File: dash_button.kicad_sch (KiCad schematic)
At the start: 55 parts, among them J1 1050570001, J2 MINI 5PTP, J3 Debug, J4 JST PH 1x2, J5 JST PH 1x5, P1 CONN_02X03, Q1 AO3401A, Q2 AO3401A, Q3 AO3401A, Q4 AO3401A, Q5 AO3401A, Q6 AO3401A, SW1 SW_Push, SW2 SW_Push, SW3 SW_Push, SW4 SW_Push, SW5 SW_Push, U1 ATtiny441-M, U2 HT7550-1

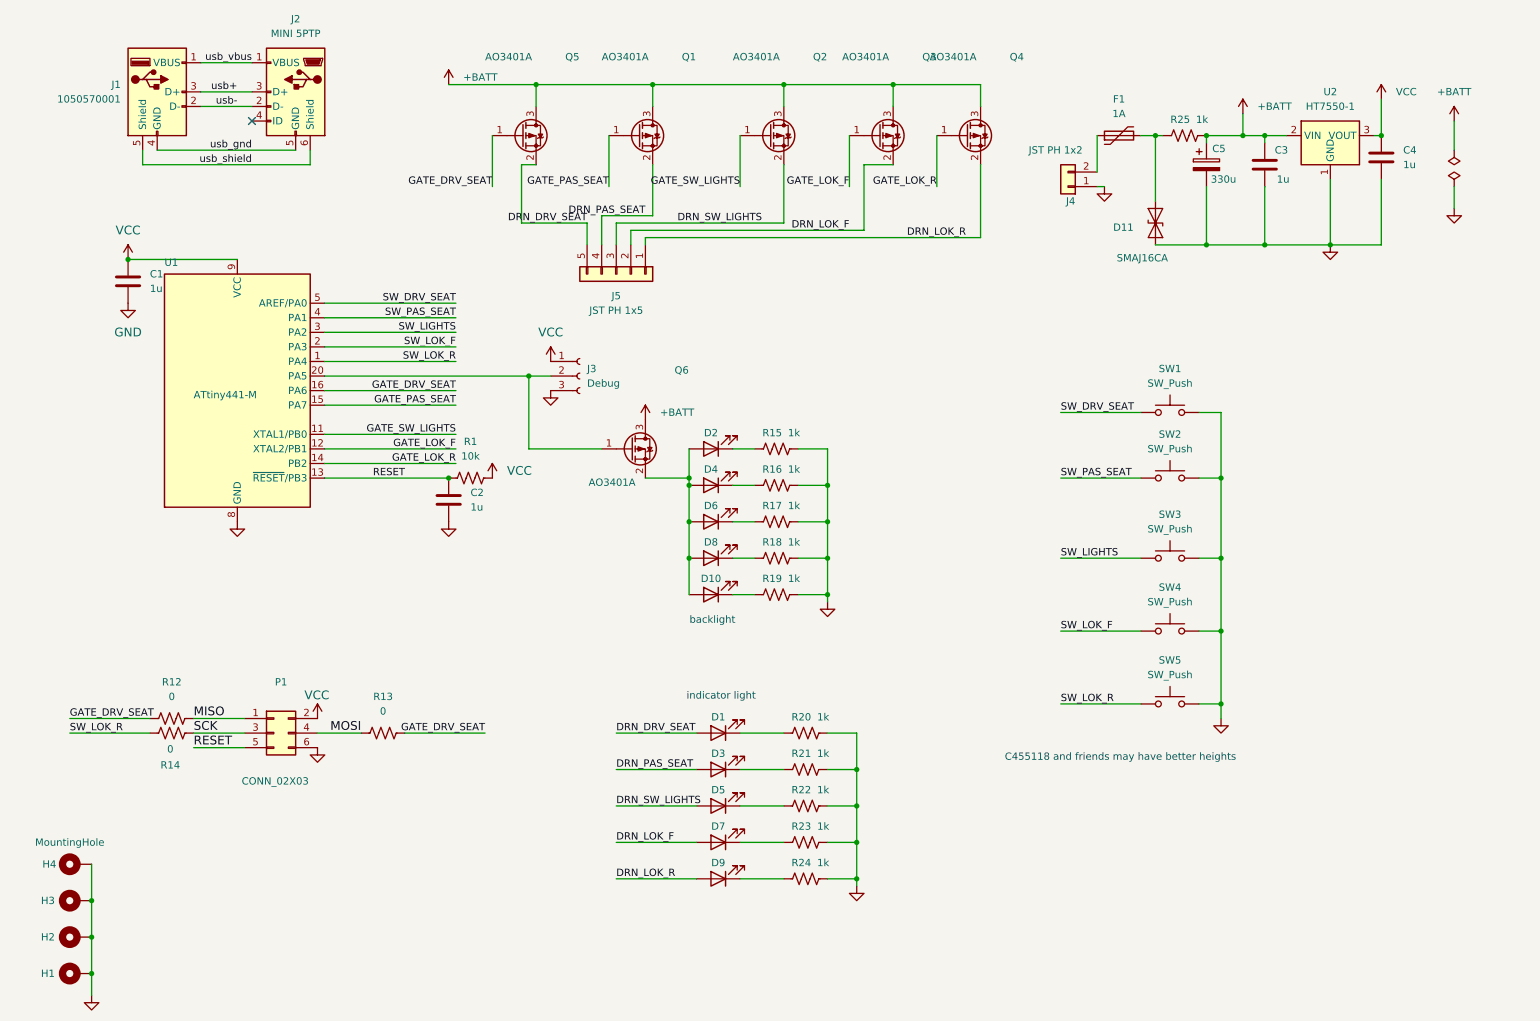
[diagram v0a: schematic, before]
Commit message: add automation for generating board_files
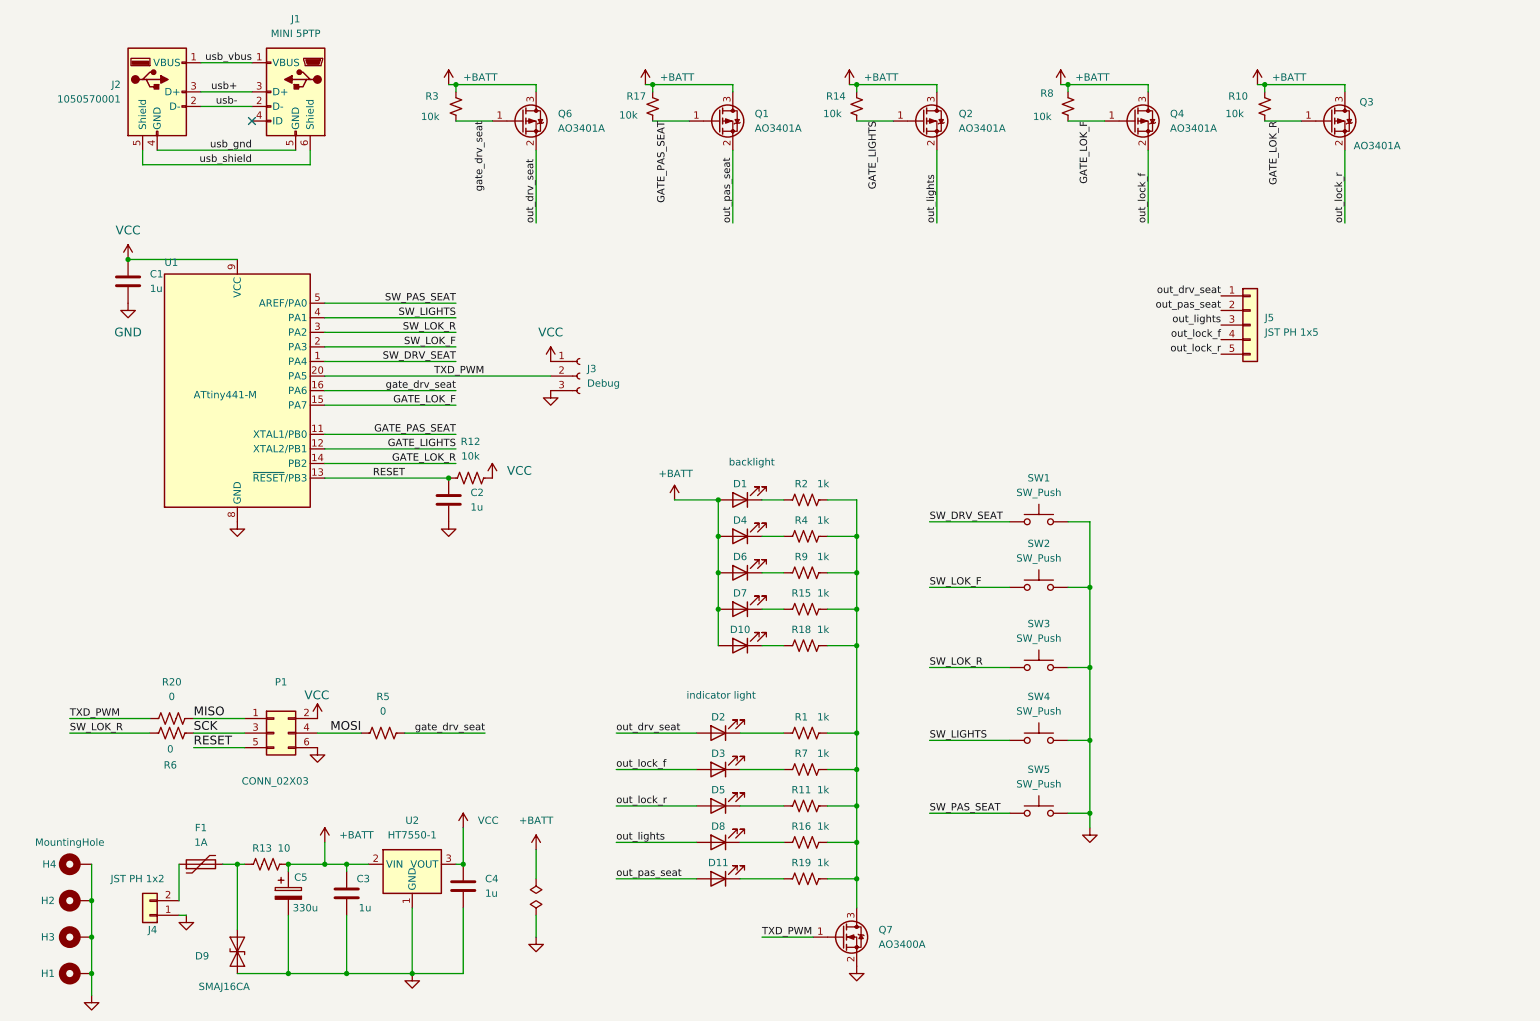
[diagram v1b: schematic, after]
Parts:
- removed Q1, Q2, Q4, Q5, Q6: AO3401A, Package_TO_SOT_SMD:SOT-23, symbol Device:Q_PMOS_GSD
- added Q1, Q2, Q4, Q6: AO3401A, Package_TO_SOT_SMD:SOT-23, symbol Transistor_FET:AO3401A
- added Q7: AO3400A, Package_TO_SOT_SMD:SOT-23, symbol Transistor_FET:AO3400A
- added R10, R14, R17, R3, R8: 10k, Resistor_SMD:R_0805_2012Metric_Pad1.20x1.40mm_HandSolder, symbol Device:R_Small_US
- Q3: Manufacturer Alpha & Omega Semicon -> Alpha & Omega Semicon
- R1: renamed from R20; footprint Resistor_SMD:R_0402_1005Metric -> Resistor_SMD:R_0805_2012Metric_Pad1.20x1.40mm_HandSolder; LCSC Part # C11702 -> C17513; MPN 0402WGF1001TCE -> 0805W8F1001T5E
- R11: renamed from R22; footprint Resistor_SMD:R_0402_1005Metric -> Resistor_SMD:R_0805_2012Metric_Pad1.20x1.40mm_HandSolder; LCSC Part # C11702 -> C17513; MPN 0402WGF1001TCE -> 0805W8F1001T5E
- R12: renamed from R1; footprint Resistor_SMD:R_0402_1005Metric -> Resistor_SMD:R_0805_2012Metric_Pad1.20x1.40mm_HandSolder; LCSC Part # C25744 -> C17414; MPN 0402WGF1002TCE -> 0805W8F1002T5E
- R13: renamed from R25; value 1k -> 10; footprint Resistor_SMD:R_0402_1005Metric -> Resistor_SMD:R_0805_2012Metric_Pad1.20x1.40mm_HandSolder; LCSC Part # C11702 -> C17415; MPN 0402WGF1001TCE -> 0805W8F100JT5E
- R15: renamed from R18; footprint Resistor_SMD:R_0402_1005Metric -> Resistor_SMD:R_0805_2012Metric_Pad1.20x1.40mm_HandSolder; LCSC Part # C11702 -> C17513; MPN 0402WGF1001TCE -> 0805W8F1001T5E
- R16: renamed from R23; footprint Resistor_SMD:R_0402_1005Metric -> Resistor_SMD:R_0805_2012Metric_Pad1.20x1.40mm_HandSolder; LCSC Part # C11702 -> C17513; MPN 0402WGF1001TCE -> 0805W8F1001T5E
- R18: renamed from R19; footprint Resistor_SMD:R_0402_1005Metric -> Resistor_SMD:R_0805_2012Metric_Pad1.20x1.40mm_HandSolder; LCSC Part # C11702 -> C17513; MPN 0402WGF1001TCE -> 0805W8F1001T5E
- R19: renamed from R24; footprint Resistor_SMD:R_0402_1005Metric -> Resistor_SMD:R_0805_2012Metric_Pad1.20x1.40mm_HandSolder; LCSC Part # C11702 -> C17513; MPN 0402WGF1001TCE -> 0805W8F1001T5E
- R2: renamed from R15; footprint Resistor_SMD:R_0402_1005Metric -> Resistor_SMD:R_0805_2012Metric_Pad1.20x1.40mm_HandSolder; LCSC Part # C11702 -> C17513; MPN 0402WGF1001TCE -> 0805W8F1001T5E
- R20: renamed from R12; footprint Resistor_SMD:R_0402_1005Metric -> Resistor_SMD:R_0805_2012Metric_Pad1.20x1.40mm_HandSolder; LCSC Part # C17168 -> C17477; MPN 0402WGF0000TCE -> 0805W8F0000T5E
- R4: renamed from R16; footprint Resistor_SMD:R_0402_1005Metric -> Resistor_SMD:R_0805_2012Metric_Pad1.20x1.40mm_HandSolder; LCSC Part # C11702 -> C17513; MPN 0402WGF1001TCE -> 0805W8F1001T5E
- R5: renamed from R13; footprint Resistor_SMD:R_0402_1005Metric -> Resistor_SMD:R_0805_2012Metric_Pad1.20x1.40mm_HandSolder; LCSC Part # C17168 -> C17477; MPN 0402WGF0000TCE -> 0805W8F0000T5E
- R6: renamed from R14; footprint Resistor_SMD:R_0402_1005Metric -> Resistor_SMD:R_0805_2012Metric_Pad1.20x1.40mm_HandSolder; LCSC Part # C17168 -> C17477; MPN 0402WGF0000TCE -> 0805W8F0000T5E
- R7: renamed from R21; footprint Resistor_SMD:R_0402_1005Metric -> Resistor_SMD:R_0805_2012Metric_Pad1.20x1.40mm_HandSolder; LCSC Part # C11702 -> C17513; MPN 0402WGF1001TCE -> 0805W8F1001T5E
- R9: renamed from R17; footprint Resistor_SMD:R_0402_1005Metric -> Resistor_SMD:R_0805_2012Metric_Pad1.20x1.40mm_HandSolder; LCSC Part # C11702 -> C17513; MPN 0402WGF1001TCE -> 0805W8F1001T5E
- U2: MPN (none) -> HT7550-1
- renumbered D2 to D1, D9 to D11, D1 to D2, D8 to D7, D7 to D8, D11 to D9, H3 to H2, H2 to H3, J2 to J1, J1 to J2
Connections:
- net GATE_SW_LIGHTS is gone; now on net GATE_PAS_SEAT: U1.11 (XTAL1/PB0)
- net +BATT: now also D1.2 (A), D10.2 (A), D4.2 (A), D6.2 (A), D7.2 (A), Q1.3 (D), Q2.3 (D), Q4.3 (D), Q6.3 (D), R10.1, R14.1, R17.1, R3.1, R8.1
- net GATE_LOK_F: now also U1.15 (PA7), Q4.1 (G), R8.2; no longer Q3.1 (G), U1.12 (XTAL2/PB1)
- net GATE_LOK_R: now also Q3.1 (G), R10.2
- net GATE_PAS_SEAT: now also Q1.1 (G), R17.2; no longer U1.15 (PA7)
- net GND: now also Q7.2 (S); no longer R1.2, R11.2, R15.2, R16.2, R18.2, R19.2, R2.2, R4.2, R7.2, R9.2
- net SW_DRV_SEAT: now also U1.1 (PA4); no longer U1.5 (AREF/PA0)
- net SW_LIGHTS: now also SW4.1, U1.4 (PA1); no longer SW3.1, U1.3 (PA2)
- net SW_LOK_F: now also SW2.1; no longer SW4.1
- net SW_LOK_R: now also SW3.1, U1.3 (PA2); no longer SW5.1, U1.1 (PA4)
- net SW_PAS_SEAT: now also SW5.1, U1.5 (AREF/PA0); no longer SW2.1, U1.4 (PA1)
- net TXD_PWM: now reaches J3.2 (Pin_2), U1.20 (PA5)
- net TXD_PWM: now also R20.2, Q7.1 (G)
- net DRN_DRV_SEAT renamed out_drv_seat
- net out_drv_seat: now also J5.1 (Pin_1), Q6.2 (S); no longer J5.5 (Pin_5)
- removed net DRN_LOK_F: D8.2 (A), J5.2 (Pin_2), Q3.2 (S)
- net DRN_LOK_R renamed out_pas_seat
- net out_pas_seat: now also J5.2 (Pin_2), Q1.2 (S); no longer J5.1 (Pin_1)
- net DRN_PAS_SEAT renamed out_lock_f
- net out_lock_f: now also Q4.2 (S)
- net DRN_SW_LIGHTS renamed out_lights
- net out_lights: now also D8.2 (A), Q2.2 (S); no longer D5.2 (A)
- net GATE_DRV_SEAT renamed gate_drv_seat
- net gate_drv_seat: now also Q6.1 (G), R3.2; no longer R20.2
- new net: Q7.3 (D), R1.2, R11.2, R15.2, R16.2, R18.2, R19.2, R2.2, R4.2, R7.2, R9.2
- new net GATE_LIGHTS: Q2.1 (G), R14.2, U1.12 (XTAL2/PB1)
- new net out_lock_r: D5.2 (A), J5.5 (Pin_5), Q3.2 (S)
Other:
- note removed: "C455118 and friends may have better heights"
- moved on the sheet: C3, C4, C5, D1, D10, D4, D6, D7, D9, F1, J4, J5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

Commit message: use nchannel mosfet + pchannel mosfet
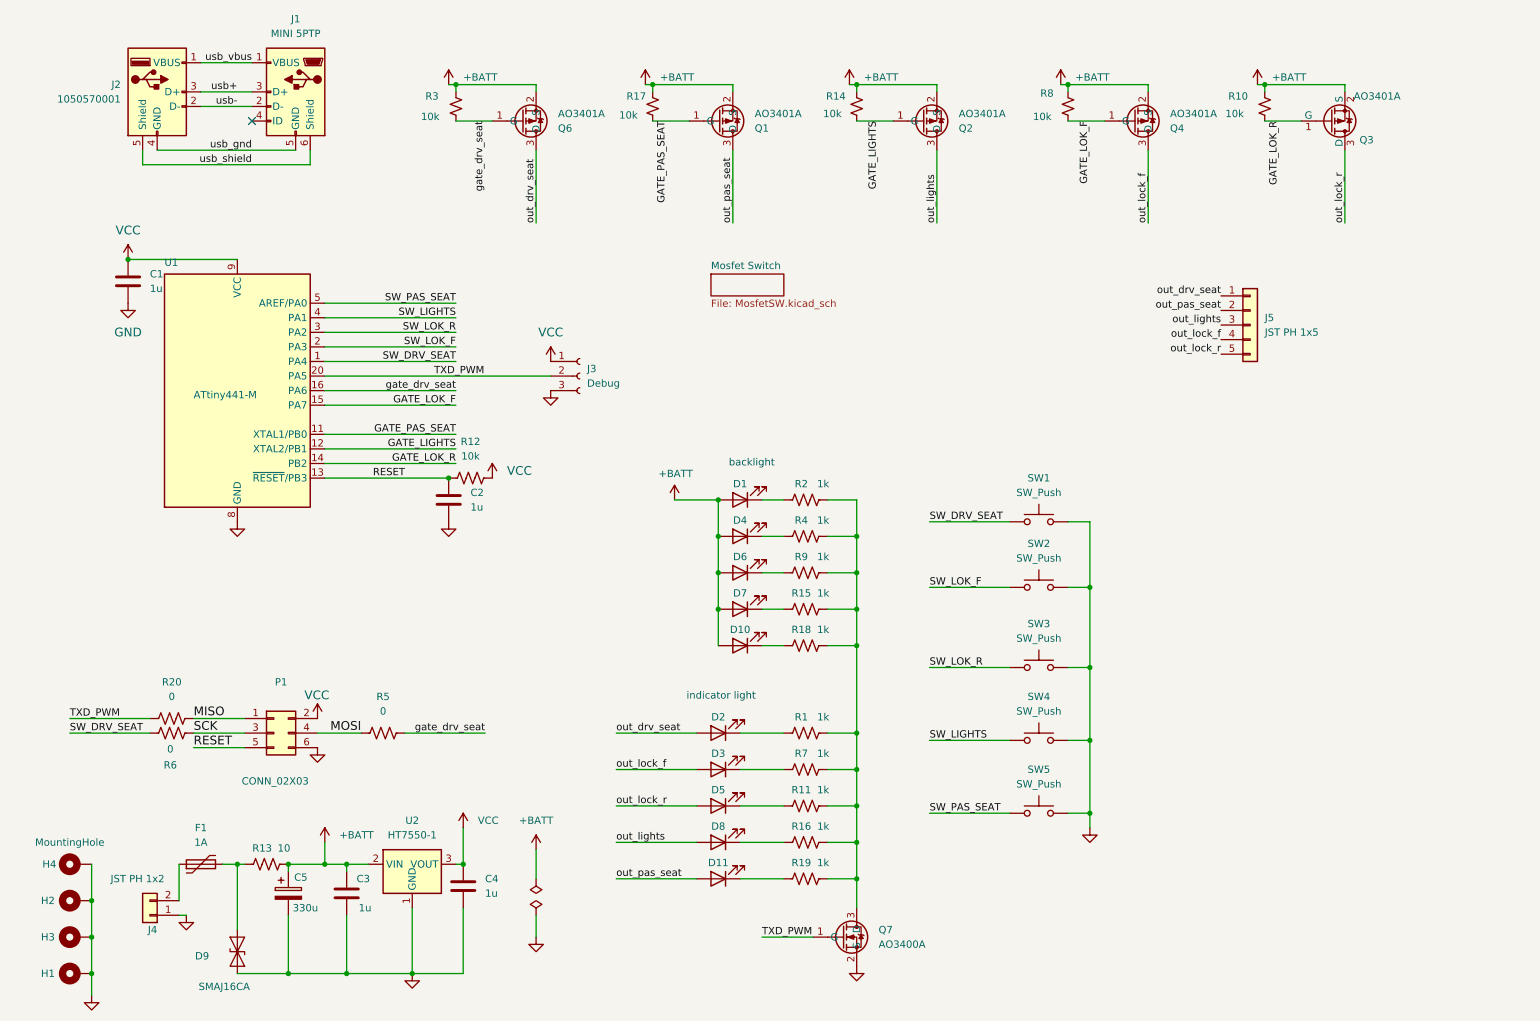
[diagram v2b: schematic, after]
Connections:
- net +BATT: now also Q1.2 (S), Q2.2 (S), Q3.2 (S), Q4.2 (S), Q6.2 (S); no longer Q1.3 (D), Q2.3 (D), Q3.3 (D), Q4.3 (D), Q6.3 (D)
- net SW_DRV_SEAT: now also R6.1
- net SW_LOK_R: no longer R6.1
- net out_drv_seat: now also Q6.3 (D); no longer Q6.2 (S)
- net out_lights: now also Q2.3 (D); no longer Q2.2 (S)
- net out_lock_f: now also Q4.3 (D); no longer Q4.2 (S)
- net out_lock_r: now also Q3.3 (D); no longer Q3.2 (S)
- net out_pas_seat: now also Q1.3 (D); no longer Q1.2 (S)
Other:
- added sheet Mosfet Switch (MosfetSW.kicad_sch)
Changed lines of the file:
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@@
 		)
 	)
+	(label "SW_DRV_SEAT"
+		(at 25.4 144.78 0)
+		(fields_autoplaced yes)
+		(effects
+			(font
+				(size 1.27 1.27)
+			)
+			(justify left bottom)
+		)
+	)
 	(label "GATE_PAS_SEAT"
 		(at 129.54 38.1 270)
@@
 		)
 	)
-	(label "SW_LOK_R"
-		(at 25.4 144.78 0)
-		(fields_autoplaced yes)
-		(effects
-			(font
-				(size 1.27 1.27)
-			)
-			(justify left bottom)
-		)
-	)
 	(label "out_drv_seat"
 		(at 226.06 68.58 180)
@@
 		(lib_id "Transistor_FET:AO3401A")
 		(at 210.82 38.1 0)
+		(mirror x)
 		(unit 1)
 		(exclude_from_sim no)
@@
 		(on_board yes)
 		(dnp no)
-		(fields_autoplaced yes)
 		(property "Reference" "Q4"
-			(at 217.17 36.8299 0)
+			(at 217.17 39.3701 0)
 			(effects
 				(font
@@
 		)
 		(property "Value" "AO3401A"
-			(at 217.17 39.3699 0)
+			(at 217.17 36.8301 0)
 			(effects
 				(font
@@
 		)
 		(property "Footprint" "Package_TO_SOT_SMD:SOT-23"
-			(at 215.9 40.005 0)
+			(at 215.9 36.195 0)
 			(effects
 				(font
@@
 		)
 		(property "Datasheet" "http://www.aosmd.com/pdfs/datasheet/AO3401A.pdf"
-			(at 215.9 41.91 0)
+			(at 215.9 34.29 0)
 			(effects
 				(font
@@
 	)
 	(symbol
+		(lib_name "AO3401A_3")
 		(lib_id "Transistor_FET:AO3401A")
 		(at 173.99 38.1 0)
+		(mirror x)
 		(unit 1)
 		(exclude_from_sim no)
@@
 		(on_board yes)
 		(dnp no)
-		(fields_autoplaced yes)
 		(property "Reference" "Q2"
-			(at 180.34 36.8299 0)
+			(at 180.34 39.3701 0)
 			(effects
 				(font
@@
 		)
 		(property "Value" "AO3401A"
-			(at 180.34 39.3699 0)
+			(at 180.34 36.8301 0)
 			(effects
 				(font
@@
 		)
 		(property "Footprint" "Package_TO_SOT_SMD:SOT-23"
-			(at 179.07 40.005 0)
+			(at 179.07 36.195 0)
 			(effects
 				(font
@@
 		)
 		(property "Datasheet" "http://www.aosmd.com/pdfs/datasheet/AO3401A.pdf"
-			(at 179.07 41.91 0)
+			(at 179.07 34.29 0)
 			(effects
 				(font
@@
 	)
 	(symbol
+		(lib_name "AO3401A_1")
 		(lib_id "Transistor_FET:AO3401A")
 		(at 104.14 38.1 0)
+		(mirror x)
 		(unit 1)
 		(exclude_from_sim no)
@@
 		(on_board yes)
 		(dnp no)
-		(fields_autoplaced yes)
 		(property "Reference" "Q6"
-			(at 110.49 36.8299 0)
+			(at 110.49 39.3701 0)
 			(effects
 				(font
@@
 		)
 		(property "Value" "AO3401A"
-			(at 110.49 39.3699 0)
+			(at 110.49 36.8301 0)
 			(effects
 				(font
@@
 		)
 		(property "Footprint" "Package_TO_SOT_SMD:SOT-23"
-			(at 109.22 40.005 0)
+			(at 109.22 36.195 0)
 			(effects
 				(font
@@
 		)
 		(property "Datasheet" "http://www.aosmd.com/pdfs/datasheet/AO3401A.pdf"
-			(at 109.22 41.91 0)
+			(at 109.22 34.29 0)
 			(effects
 				(font
@@
 		(lib_id "Device:Q_PMOS_GSD")
 		(at 245.11 38.1 0)
+		(mirror x)
 		(unit 1)
 		(exclude_from_sim no)
@@
 		(dnp no)
 		(property "Reference" "Q3"
-			(at 250.19 34.798 0)
+			(at 250.19 41.402 0)
 			(effects
 				(font
@@
 		)
 		(property "Value" "AO3401A"
-			(at 249.174 42.418 0)
+			(at 249.174 33.782 0)
 			(effects
 				(font
@@
 		)
 		(property "Footprint" "Package_TO_SOT_SMD:SOT-23"
-			(at 250.19 35.56 0)
+			(at 250.19 40.64 0)
 			(effects
 				(font
@@
 	)
 	(symbol
+		(lib_name "AO3401A_2")
 		(lib_id "Transistor_FET:AO3401A")
 		(at 138.43 38.1 0)
+		(mirror x)
 		(unit 1)
 		(exclude_from_sim no)
@@
 		(on_board yes)
 		(dnp no)
-		(fields_autoplaced yes)
 		(property "Reference" "Q1"
-			(at 144.78 36.8299 0)
+			(at 144.78 39.3701 0)
 			(effects
 				(font
@@
 		)
 		(property "Value" "AO3401A"
-			(at 144.78 39.3699 0)
+			(at 144.78 36.8301 0)
 			(effects
 				(font
@@
 		)
 		(property "Footprint" "Package_TO_SOT_SMD:SOT-23"
-			(at 143.51 40.005 0)
+			(at 143.51 36.195 0)
 			(effects
 				(font
@@
 		)
 		(property "Datasheet" "http://www.aosmd.com/pdfs/datasheet/AO3401A.pdf"
-			(at 143.51 41.91 0)
+			(at 143.51 34.29 0)
 			(effects
 				(font
@@
 				)
 			)
+		)
+	)
+	(sheet
+		(at 137.16 64.77)
+		(size 12.7 3.81)
+		(fields_autoplaced yes)
+		(stroke
+			(width 0.1524)
+			(type solid)
+		)
+		(fill
+			(color 0 0 0 0.0000)
+		)
+		(property "Sheetname" "Mosfet Switch"
+			(at 137.16 64.0584 0)
+			(effects
+				(font
+					(size 1.27 1.27)
+				)
+				(justify left bottom)
+			)
+		)
+		(property "Sheetfile" "MosfetSW.kicad_sch"
+			(at 137.16 69.1646 0)
+			(effects
+				(font
+					(size 1.27 1.27)
+				)
+				(justify left top)
+			)
+		)
+		(instances
+			(project "dash_button"
+				(path "/b08ccec5-125a-434b-8920-b67dba6607ba"
+					(page "2")
+				)
+			)
